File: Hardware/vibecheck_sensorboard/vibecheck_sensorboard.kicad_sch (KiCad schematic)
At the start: 9 parts, among them J101 Conn_01x08

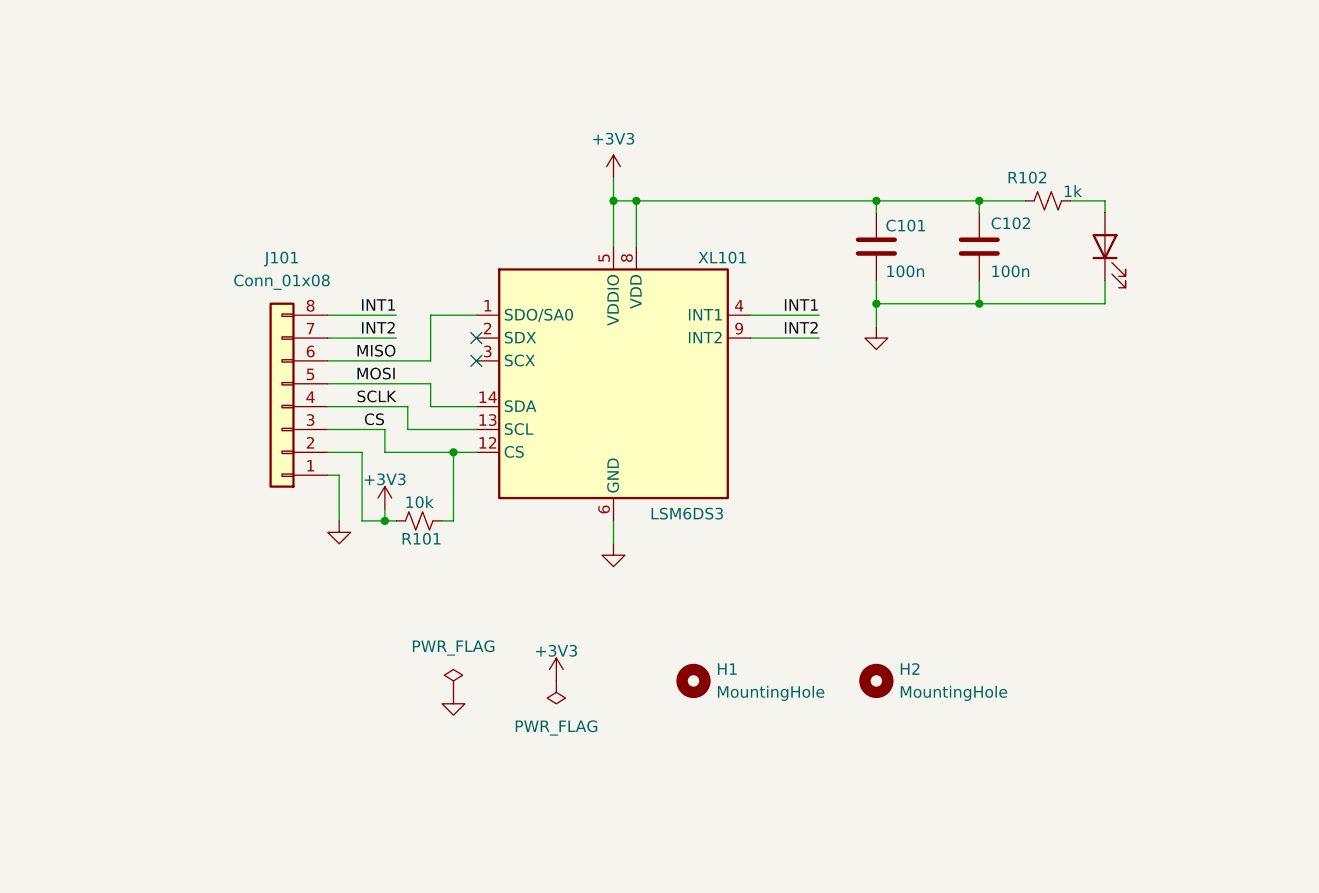
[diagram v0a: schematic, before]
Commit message: updated folder and file names, added README
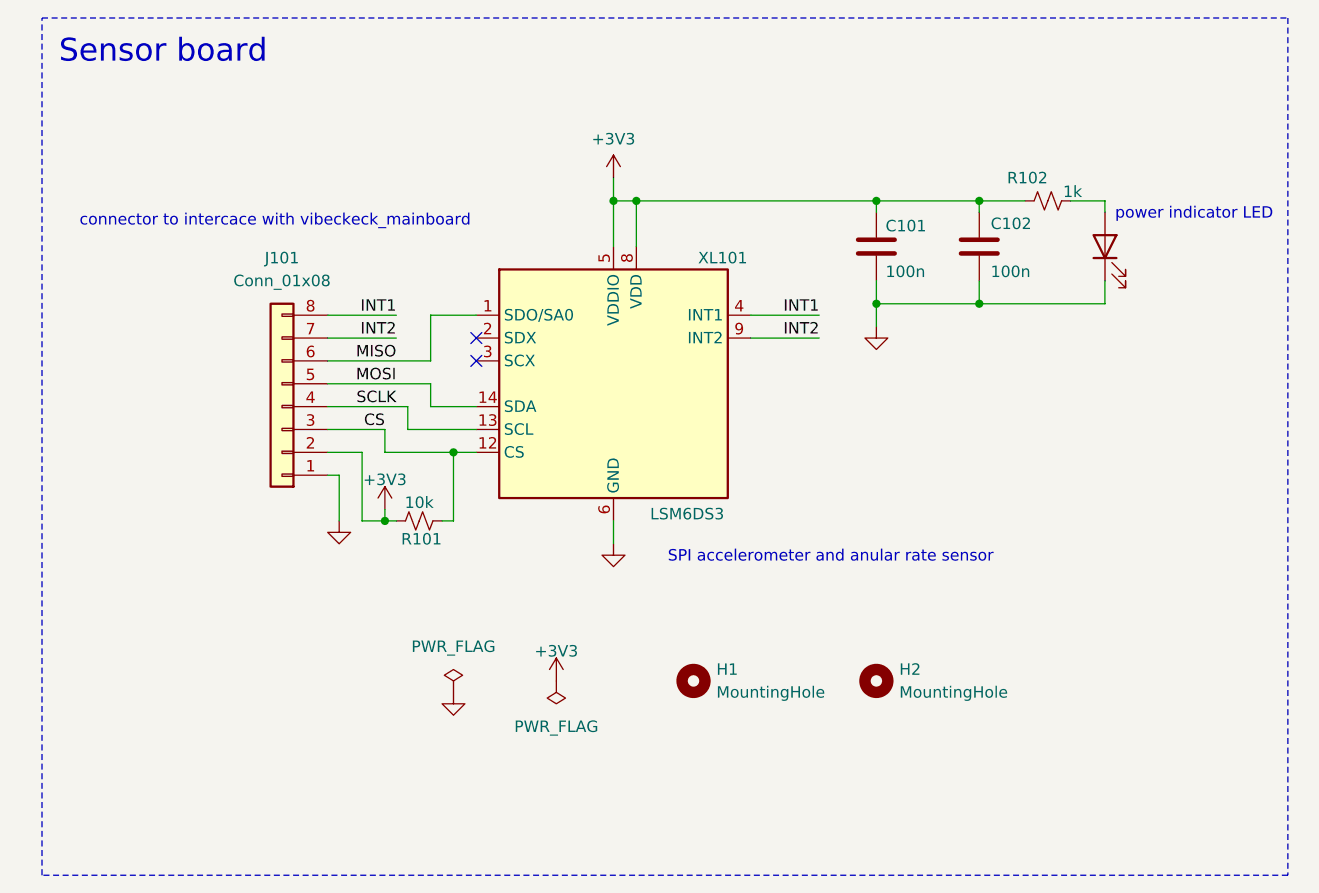
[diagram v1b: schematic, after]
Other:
- note added: "SPI accelerometer and anular rate sensor"
- note added: "Sensor board"
- note added: "connector to intercace with vibeckeck_mainboard"
- note added: "power indicator LED"
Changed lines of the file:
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@@
+		)
+	)
+	(rectangle
+		(start 71.12 53.34)
+		(end 209.55 148.59)
+		(stroke
+			(width 0)
+			(type dash)
+		)
+		(fill
+			(type none)
+		)
+	)
+	(text "connector to intercace with vibeckeck_mainboard"
+		(exclude_from_sim no)
+		(at 97.028 75.946 0)
+		(effects
+			(font
+				(size 1.27 1.27)
+			)
+		)
+	)
+	(text "SPI accelerometer and anular rate sensor"
+		(exclude_from_sim no)
+		(at 158.75 113.284 0)
+		(effects
+			(font
+				(size 1.27 1.27)
+			)
+		)
+	)
+	(text "power indicator LED"
+		(exclude_from_sim no)
+		(at 199.136 75.184 0)
+		(effects
+			(font
+				(size 1.27 1.27)
+			)
+		)
+	)
+	(text "Sensor board"
+		(exclude_from_sim no)
+		(at 84.582 57.15 0)
+		(effects
+			(font
+				(size 2.54 2.54)
+			)
 		)
 	)

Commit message: added board schematics, screenshots and 3D models
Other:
- note added: "SPI accelerometer and angular rate sensor"
- note removed: "SPI accelerometer and anular rate sensor"
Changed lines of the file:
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@@
 		)
 	)
-	(text "SPI accelerometer and anular rate sensor"
+	(text "SPI accelerometer and angular rate sensor"
 		(exclude_from_sim no)
 		(at 158.75 113.284 0)
